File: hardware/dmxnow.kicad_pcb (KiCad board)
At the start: 2 copper layers, 146 x 64 mm, 76 parts, among them J1 WAGO 2604-1102 (L N in), J2 DMX tail (1 GND 2 B 3 A), J3 PROG (3V3 GND D- D+ EN BOOT), J4 WAGO 2604-1102 (L_SW N out 1), J5 WAGO 2604-1102 (VLED_IN GND_L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, J6 WAGO 2604-1105 (VLED CH1-CH4), J7 WAGO 2604-1102 (L_SW N out 2,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, K1 G5RL-1A-E-HR DC5, Q1 AO3400A, Q2 AOD2610E, Q3 AOD2610E, Q4 AOD2610E, Q5 AOD2610E, SW1 PTS810 (BOOT/maintenance), U1 ESP32-C3-MINI-1-N4, U2 SP3485EN, U3 AP2112K-3.3, U4 74AHCT125

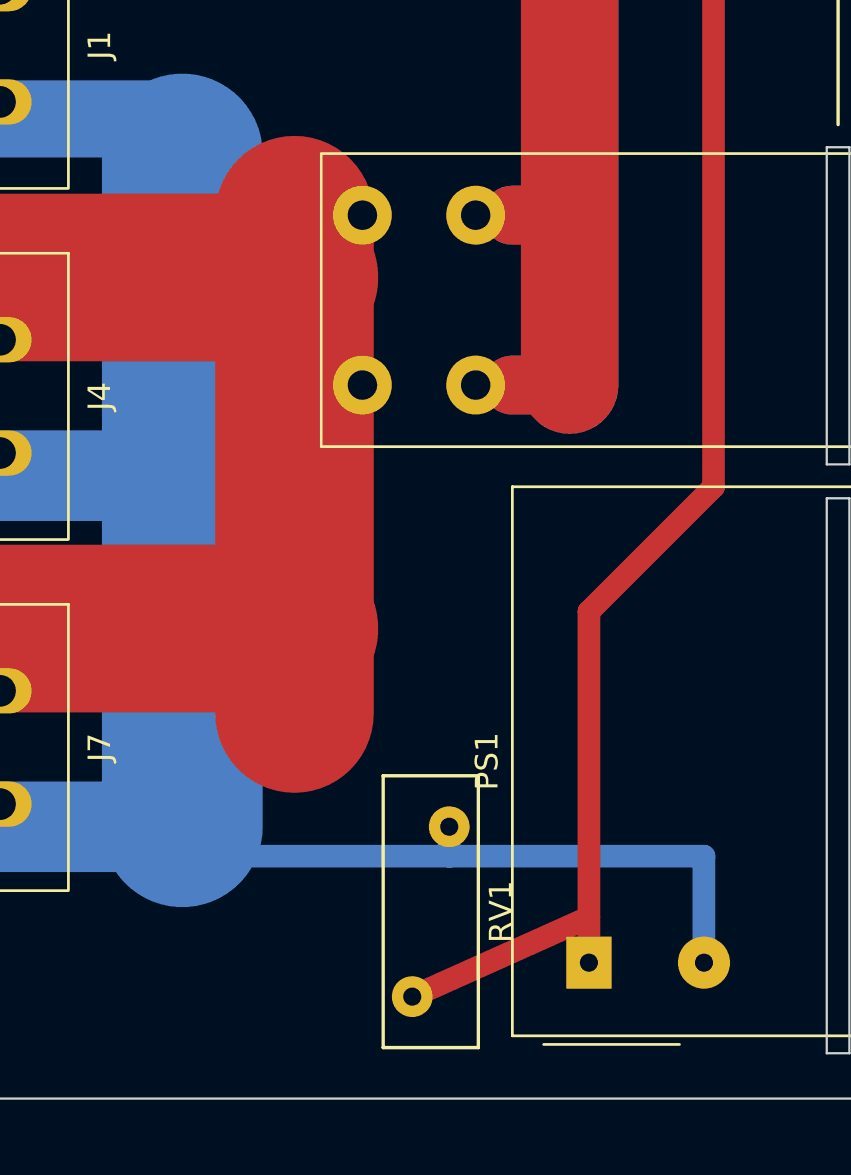
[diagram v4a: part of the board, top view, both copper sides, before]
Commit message: hardware: troisième passe de revue (RV1, canari KiCad 9, centre K1)
- RV1 : empreinte du projet, perçage 1,1 mm (pattes 0,8 +-0,1 mm, le 0,8 mm
  de KiCad était trop juste avec la tolérance JLCPCB) et corps jusqu'à 9 mm
  d'épaisseur (fiche HEL 10D) ; RV1 décalé à X = 28,5, bus L_SW raccourci.
- drc_canary.py : constante d'unités renommée dans KiCad 9 (échec CI).
- CPL : centre de K1 = centre des broches (empreinte JLC).
- REVIEW.md : RV1, découplage 3V3 et pistes d'alimentation à 0,2 mm,
  découpage du plan de masse en face arrière (points de la 3e passe).

Contrôles locaux : netlist 0 erreur, PCB 0 erreur, DRC 0 erreur /
0 non connecté, canari OK.

Co-Authored-By: Claude Opus 5.5 <noreply@anthropic.com>
Claude-Session: https://claude.ai/code/session_01B51M6ZY5abLxTmcevvc8Le
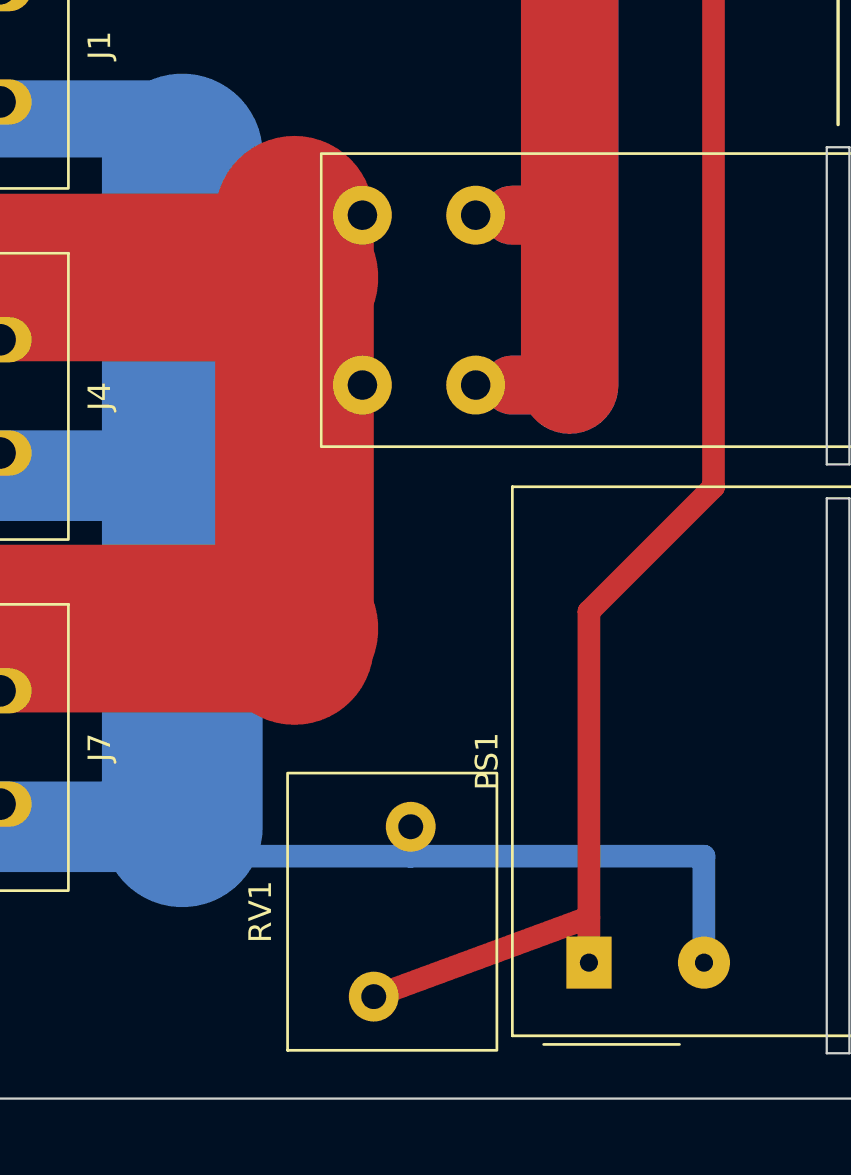
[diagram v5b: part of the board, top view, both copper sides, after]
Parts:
- RV1: footprint Varistor:RV_Disc_D12mm_W4.2mm_P7.5mm -> dmxnow:RV_Disc_D12mm_T9mm_P7.5mm_Drill1.1
- moved RV1 1.70 mm to (78.5, 99.5)
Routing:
- net L_SW: track 77.4 -> 74.4 mm
- net L_PSU: track 71.3 -> 72.9 mm

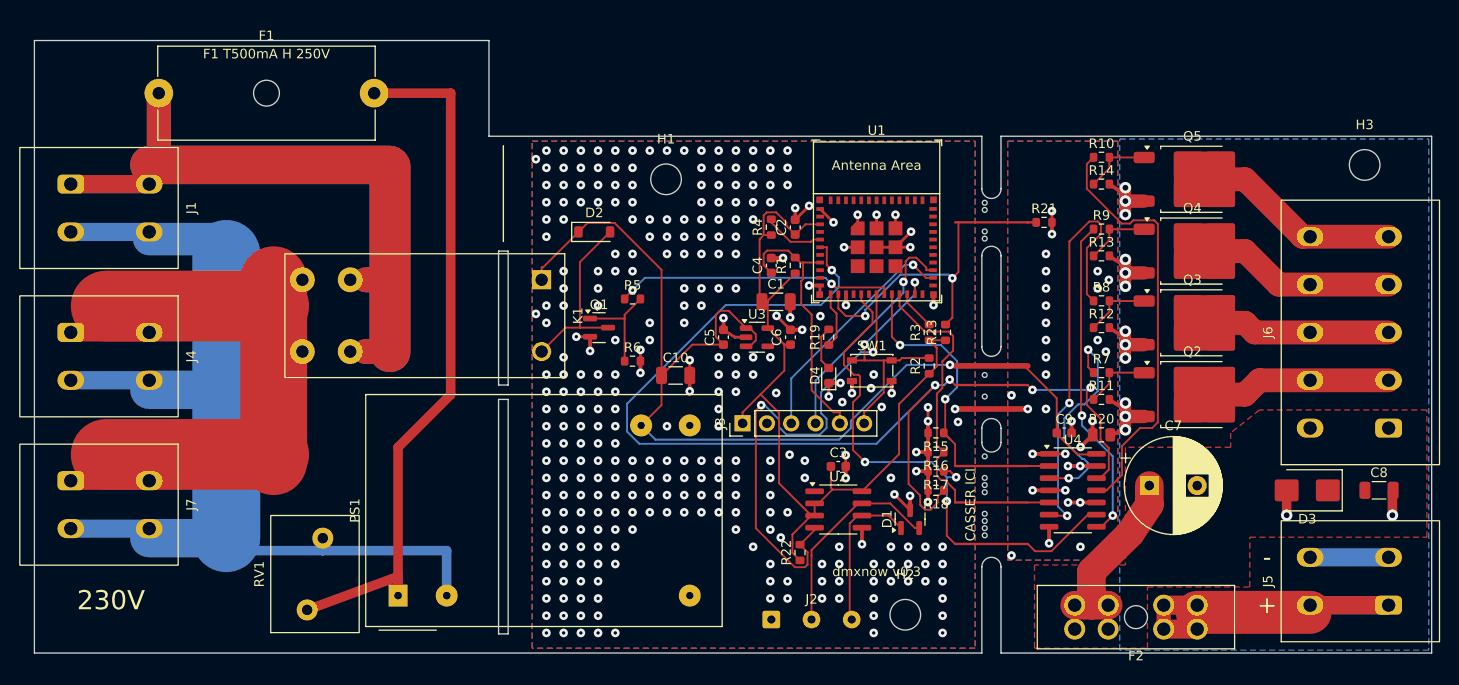
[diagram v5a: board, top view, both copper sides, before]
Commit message: hardware: quatrième passe de revue (PS1, RV1, J6, fentes, marquages)
- PS1 : empreinte du projet, perçages 1,0 mm (broches 0,6 +-0,1 mm).
- RV1 : classé traversant (il figurait dans la BOM CMS), centre CPL entre
  les pattes.
- J6 (0 stock JLCPCB) retiré des fichiers d'assemblage JLCPCB, signalé dans
  bom_full.csv.
- Fentes d'isolement 1,2 mm à bouts arrondis ; bande F1 portée à 11,5 mm
  (support de 10,8 mm) ; traits de sérigraphie >= 0,15 mm.
- Marquages : IN/OUT L/N sur J1/J4/J7, GND B- A+ sur J2, V+ 1-4 sur J6.
- REVIEW.md §7 (commande et montage), SPEC : charge rubans <= 16 A.

Contrôles : netlist 0, PCB 0, DRC 0 erreur / 0 non connecté, canari OK.

Co-Authored-By: Claude Opus 5.5 <noreply@anthropic.com>
Claude-Session: https://claude.ai/code/session_01B51M6ZY5abLxTmcevvc8Le
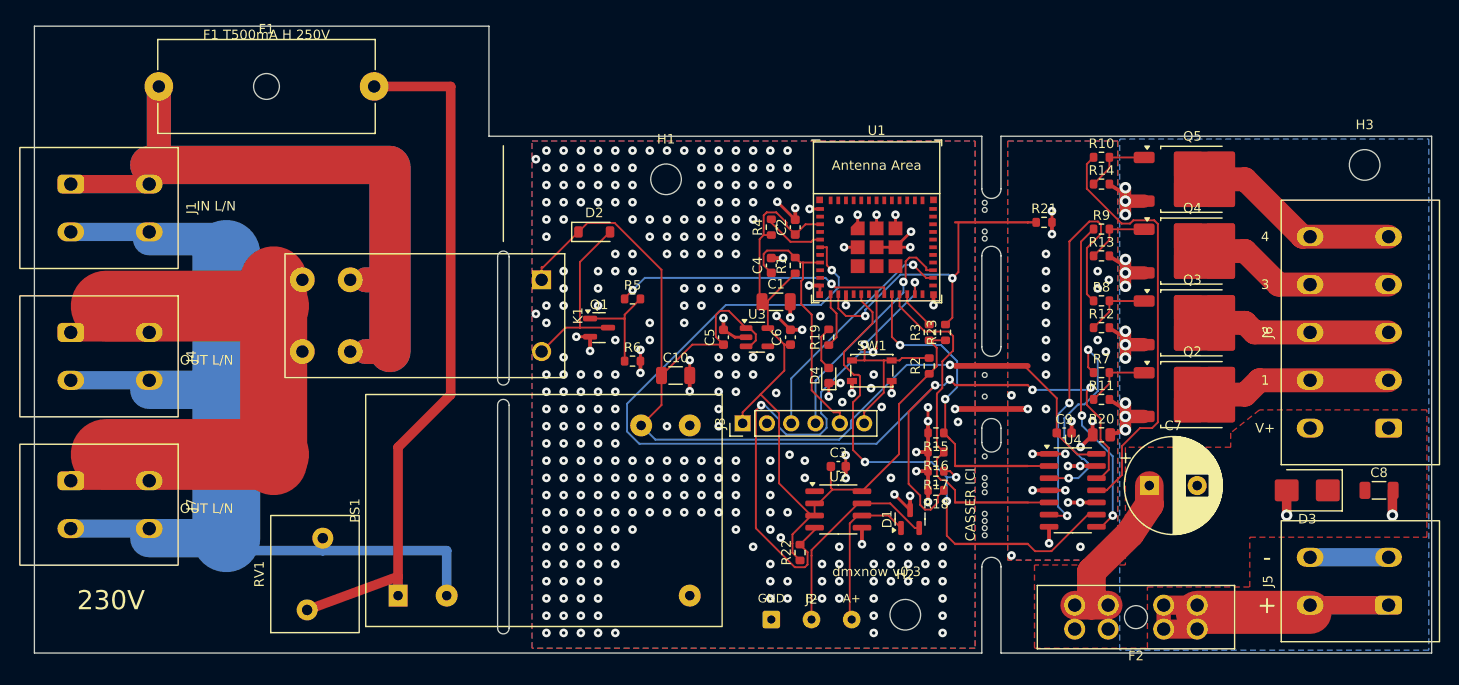
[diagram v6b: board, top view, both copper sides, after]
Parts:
- PS1: footprint Converter_ACDC:Converter_ACDC_MeanWell_IRM-03-xx_THT -> dmxnow:Converter_ACDC_MeanWell_IRM-03-xx_THT_Drill1.0
- moved F1 0.70 mm to (63.0, 44.8)
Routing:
- net L_IN: track 134.5 -> 135.9 mm
- net L_PSU: track 72.9 -> 73.6 mm
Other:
- board size 146 x 64 mm -> 146 x 65.5 mm
- board text added: "1"
- board text added: "2"
- board text added: "3"
- board text added: "4"
- board text added: "A+"
- board text added: "B-"
- board text added: "GND"
- board text added: "IN L/N"
- board text added: "OUT L/N"
- board text added: "V+"

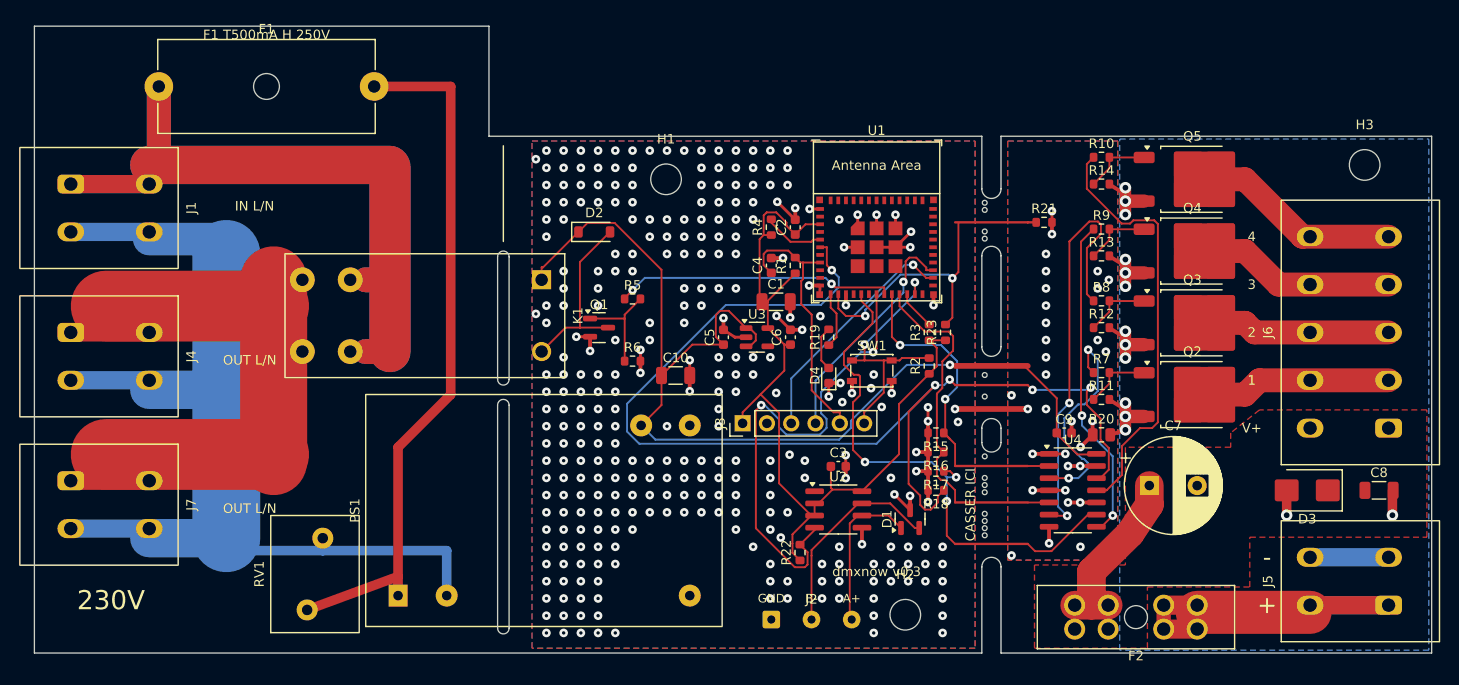
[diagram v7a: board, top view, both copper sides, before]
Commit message: hardware: cinquième passe de revue (J3 +5V, LED rouge, R15-R18, notes de commande)
- J3 passe à 7 pastilles : +5V (entrée de U3) pour programmer hors secteur sans
  réalimenter la sortie de l'AP2112K ; marquages 3V3 / 5V
- D4 LED rouge KT-0603R (C2286) + R19 330R : une LED verte VF 3,1 V ne s'allume pas
- R15-R18 décalées de 0,5 mm (4 mm sans composant de chaque côté de la découpe)
- marquages J2 en 1,0 mm ; références F1 / F2 ramenées sur la carte
- vias d'îlot : anneau entier dans les deux plans (plus de via à cheval sur un bord)
- SPEC : courant TX 350 mA, question J3-3V3 close, risque R-16 (OVP IRM-03 / AP2112K)
- README / REVIEW : 2 designs chez JLCPCB, remarque de commande complète, J6 arrêté chez WAGO

Co-Authored-By: Claude Opus 5.5 <noreply@anthropic.com>
Claude-Session: https://claude.ai/code/session_01B51M6ZY5abLxTmcevvc8Le
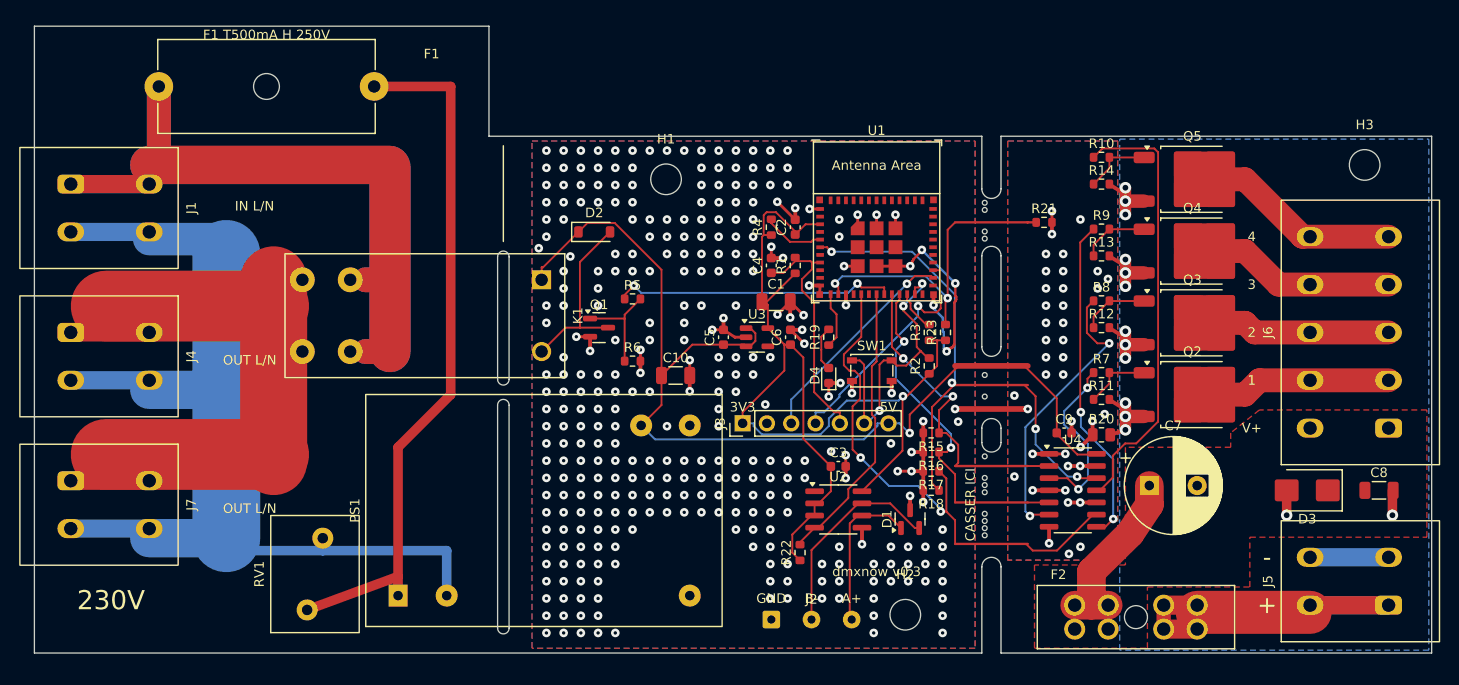
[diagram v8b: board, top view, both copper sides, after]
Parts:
- D4: value LED green 0603 -> LED red 0603
- J3: value PROG (3V3 GND D- D+ EN BOOT) -> PROG (3V3 GND D- D+ EN BOOT 5V); footprint Connector_PinHeader_2.54mm:PinHeader_1x06_P2.54mm_Vertical -> Connector_PinHeader_2.54mm:PinHeader_1x07_P2.54mm_Vertical
- R19: value 100R -> 330R
- moved R15 0.50 mm to (143.7, 81.0)
- moved R16 0.50 mm to (143.7, 83.0)
- moved R17 0.50 mm to (143.7, 85.0)
- moved R18 0.50 mm to (143.7, 87.0)
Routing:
- net PWM4: track 117.1 -> 60.3 mm, vias 5 -> 4
- net GND: track 98.5 -> 120.3 mm, vias 337 -> 364
- net DMX_TX: track 51.3 -> 30.0 mm, vias 2 -> 0
- net +3V3: track 89.8 -> 105.4 mm, vias 0 -> 1
- net DRV2: track 44.7 -> 30.3 mm
- net BOOT: track 27.2 -> 31.3 mm, vias 2 -> 3
- net DRV1: track 22.8 -> 18.7 mm
- net +5V: track 111.7 -> 108.6 mm
- net EN: track 27.8 -> 25.3 mm
- net USB_DM: track 25.0 -> 22.7 mm
- net PWM1: track 35.1 -> 33.1 mm
- net BOARD_SENSE: track 35.8 -> 33.8 mm
- net DRV4: track 44.7 -> 46.2 mm
- net PWM2: track 37.7 -> 36.5 mm, vias 0 -> 2
- net PWM3: track 56.8 -> 56.1 mm, vias 3 -> 2
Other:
- board text added: "3V3"
- board text added: "5V"
